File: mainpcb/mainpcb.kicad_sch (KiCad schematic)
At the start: 16 parts, among them J1 Raspberry_Pi_2_3, J13 Screw_Terminal_01x09, J15 Screw_Terminal_01x02, J2 8P8C_Shielded, J3 8P8C_Shielded, J4 Screw_Terminal_01x09, J9 Screw_Terminal_01x02, U1 TCA9517ADGK, U2 TXB0108PW

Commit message: Continued control board layout
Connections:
- net DSCL1+: now also J2.4; no longer J2.5
- net DSCL1-: now also J2.3; no longer J2.6
- net DSCL2+: now also J3.4; no longer J3.5
- net DSCL2-: now also J3.3; no longer J3.6
- net DSDA1+: now also J2.5; no longer J2.3
- net DSDA1-: now also J2.6; no longer J2.4
- net DSDA2+: now also J3.5; no longer J3.3
- net DSDA2-: now also J3.6; no longer J3.4
- net GND: now also J13.2 (Pin_2), J13.9 (Pin_9), J4.2 (Pin_2), J4.9 (Pin_9); no longer J13.1 (Pin_1), J4.1 (Pin_1)
- net at J13.3 (Pin_3): now also U2.14 (B6); no longer U2.12 (B8)
- net at J13.7 (Pin_7): now also U2.12 (B8); no longer U2.14 (B6)
- net at U2.15 (B5): now also J13.1 (Pin_1); no longer J13.9 (Pin_9)
- net at U2.16 (B4): now also J4.7 (Pin_7); no longer J4.3 (Pin_3)
- net at U2.18 (B2): now also J4.3 (Pin_3); no longer J4.7 (Pin_7)
- net at U2.20 (B1): now also J4.1 (Pin_1); no longer J4.9 (Pin_9)
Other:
- moved on the sheet: J13, J4

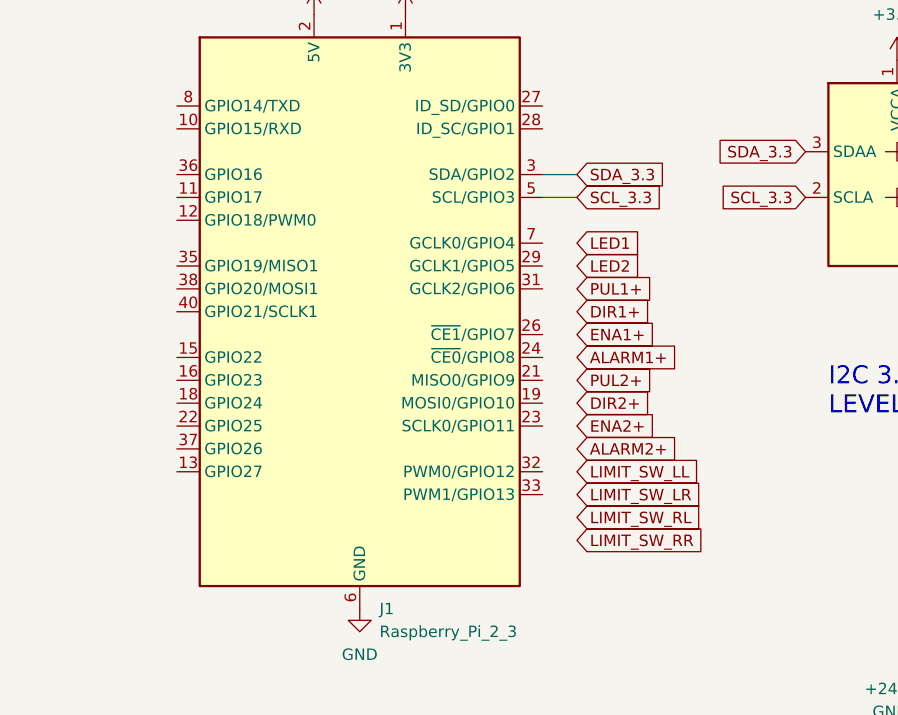
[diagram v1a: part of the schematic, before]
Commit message: Started signal track layout of control PCB
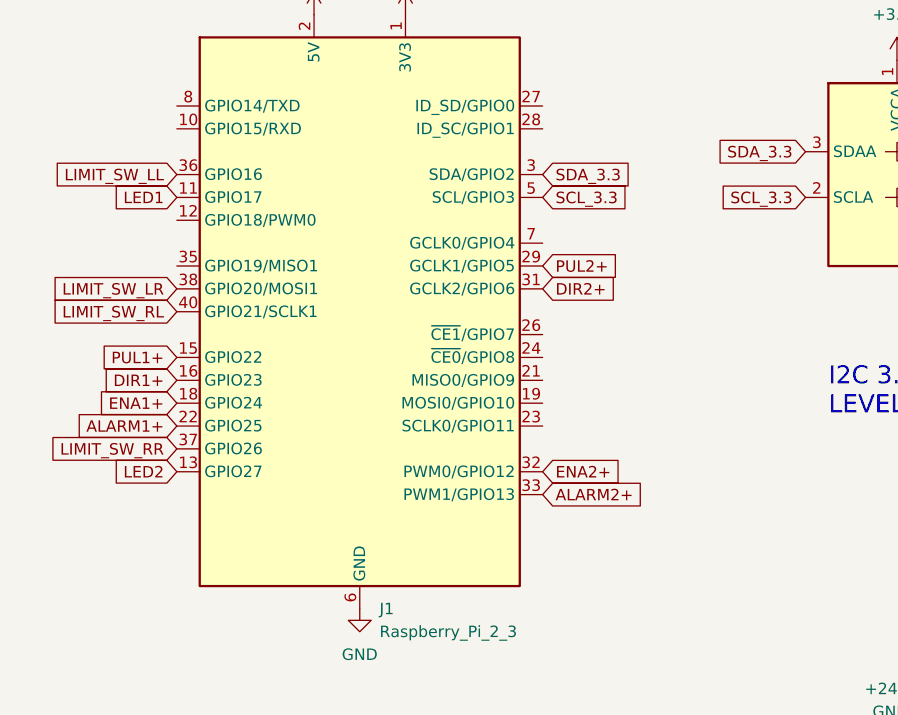
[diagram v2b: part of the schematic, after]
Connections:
- net ALARM1+: now also J1.22 (GPIO25)
- net ALARM2+: now also J1.33 (PWM1/GPIO13)
- net DIR1+: now also J1.16 (GPIO23)
- net DIR2+: now also J1.31 (GCLK2/GPIO6)
- net ENA1+: now also J1.18 (GPIO24)
- net ENA2+: now also J1.32 (PWM0/GPIO12)
- net LED1: now also J1.11 (GPIO17)
- net LED2: now also J1.13 (GPIO27)
- net LIMIT_SW_LL: now also J1.36 (GPIO16)
- net LIMIT_SW_LR: now also J1.38 (GPIO20/MOSI1)
- net LIMIT_SW_RL: now also J1.40 (GPIO21/SCLK1)
- net LIMIT_SW_RR: now also J1.37 (GPIO26)
- net PUL1+: now also J1.15 (GPIO22)
- net PUL2+: now also J1.29 (GCLK1/GPIO5)

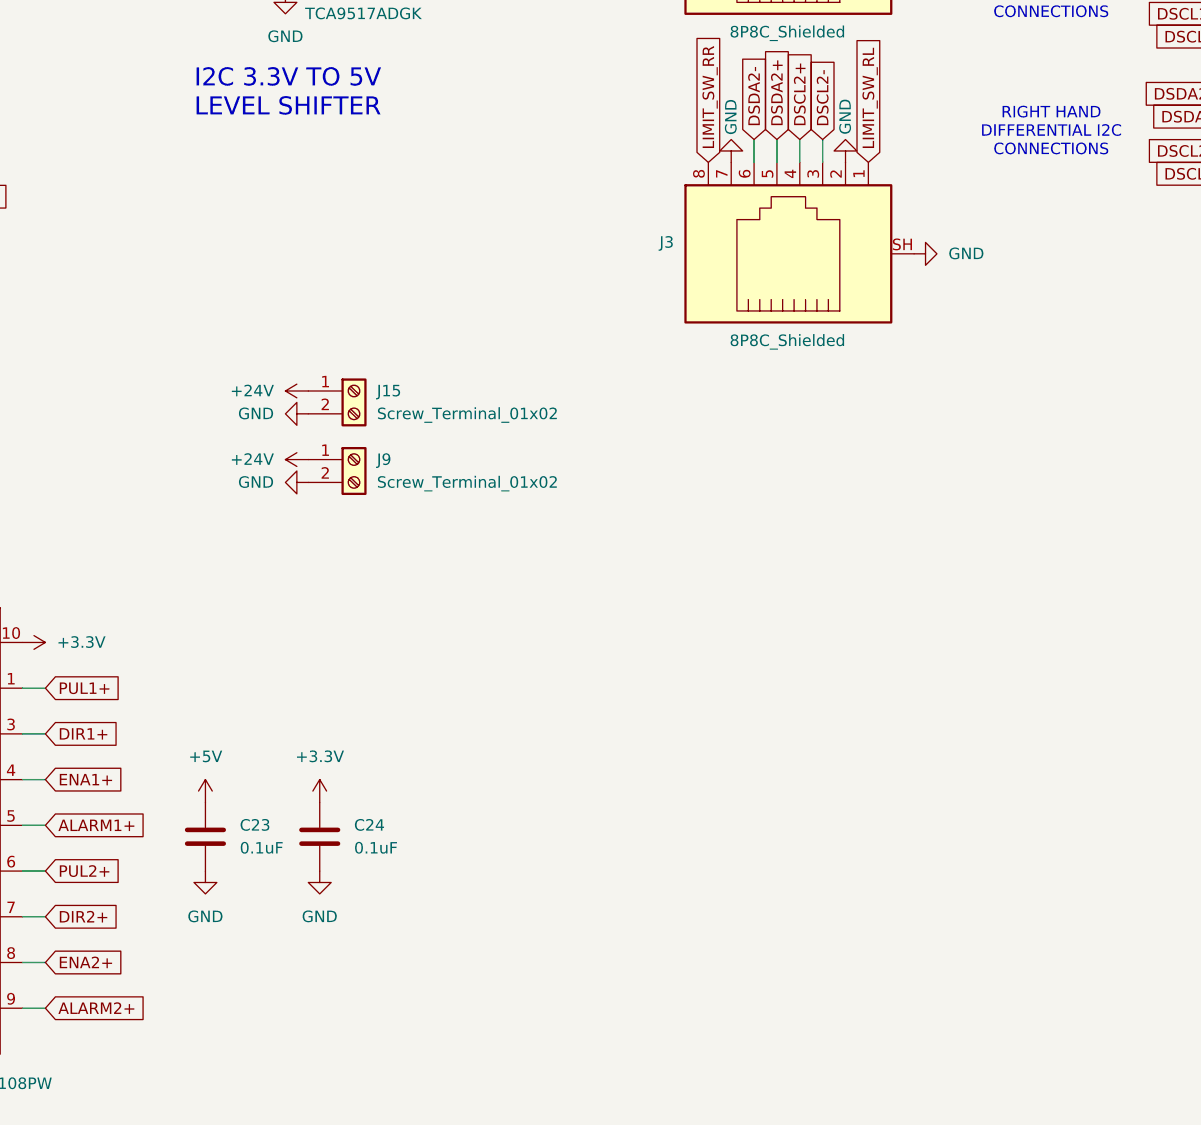
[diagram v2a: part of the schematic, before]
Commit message: Completed control board layout
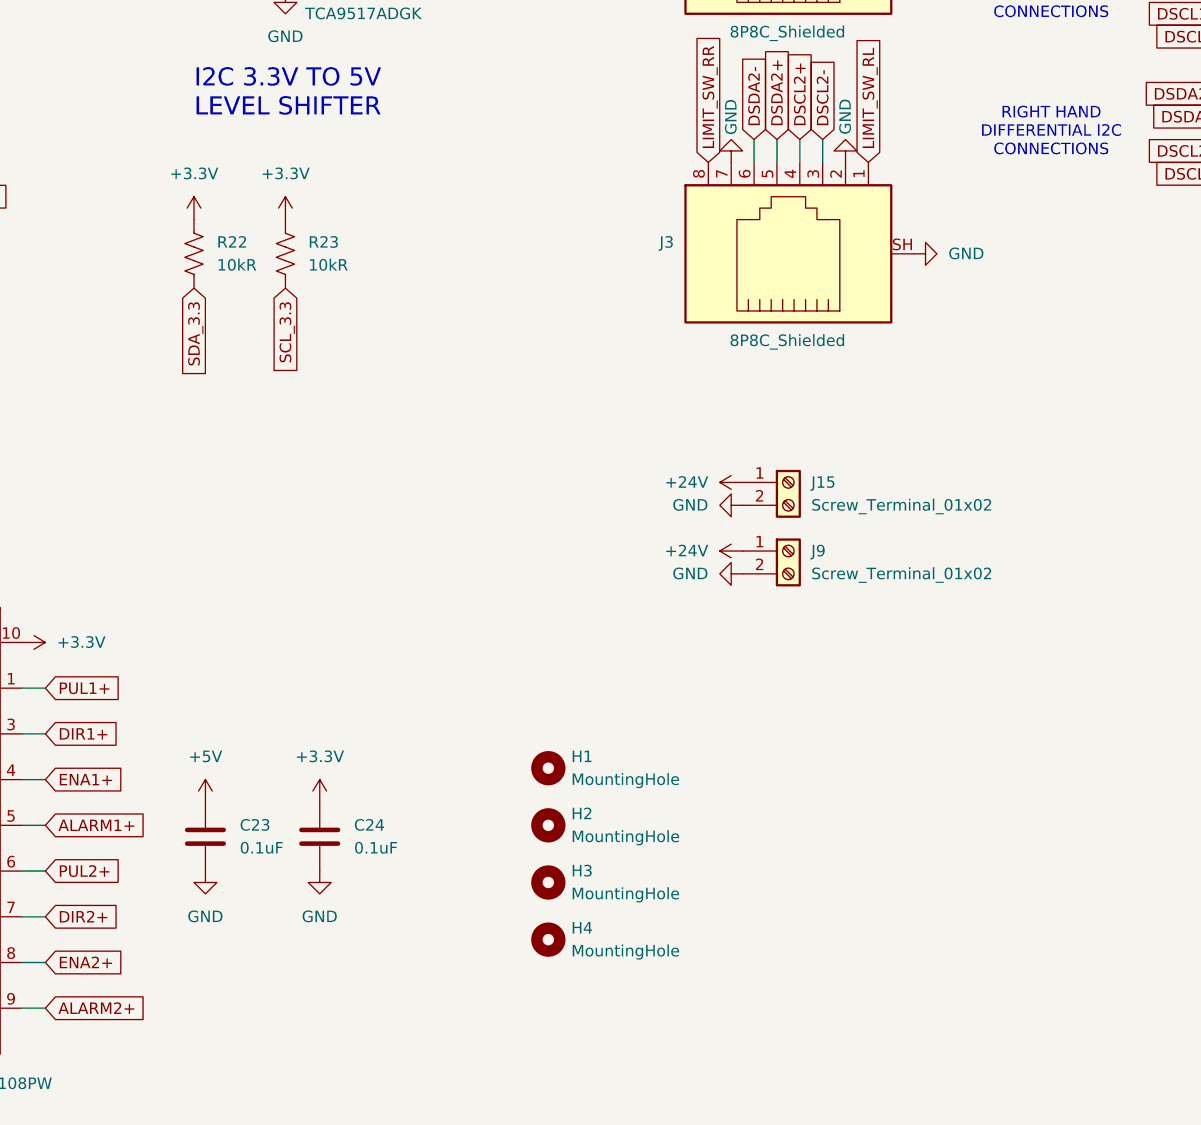
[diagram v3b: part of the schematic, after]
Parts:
- added H1, H2, H3, H4: MountingHole, MountingHole:MountingHole_4.3mm_M4, symbol Mechanical:MountingHole
- added R22, R23: 10kR, Resistor_THT:R_Axial_DIN0207_L6.3mm_D2.5mm_P10.16mm_Horizontal, symbol Device:R_US
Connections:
- net +3.3V: now also R22.1, R23.1
- net SCL_3.3: now also R23.2
- net SDA_3.3: now also R22.2
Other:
- moved on the sheet: J15, J9

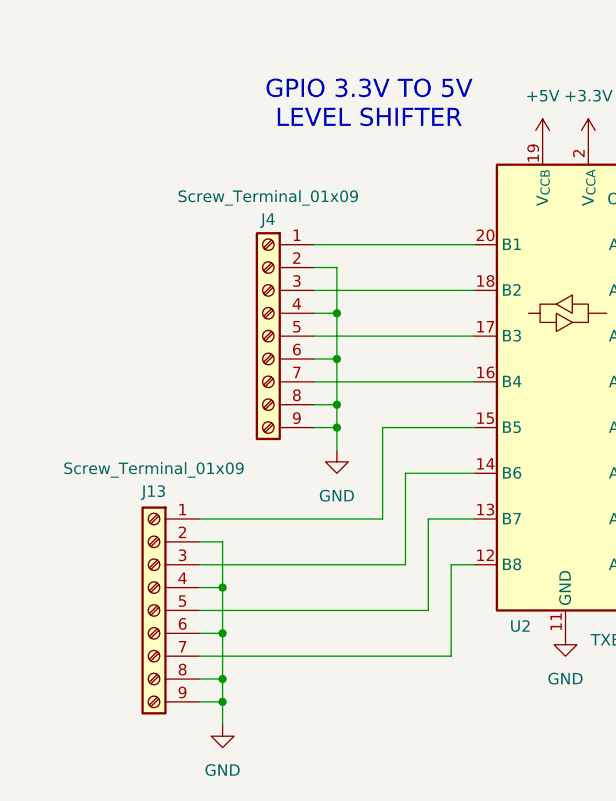
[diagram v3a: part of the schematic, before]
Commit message: As-Produced commit
This commit contains the PCBs as they were sent to the manufacturer
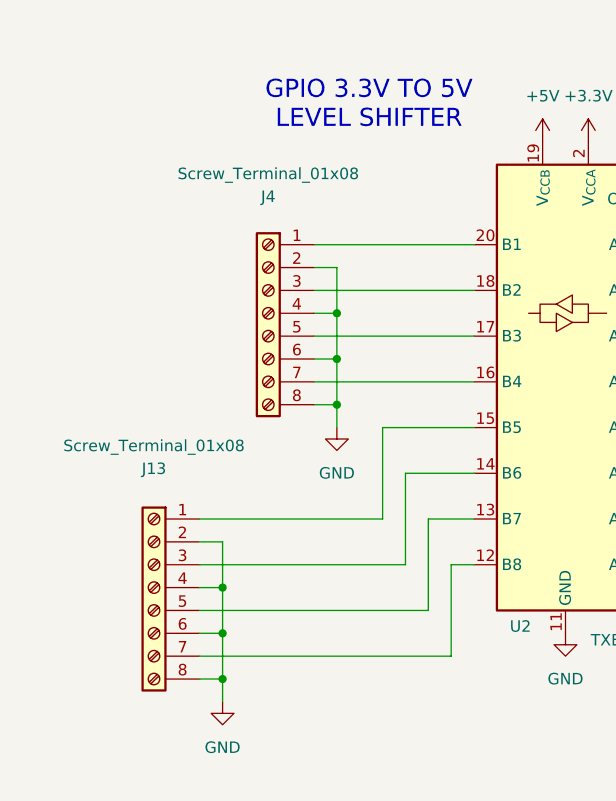
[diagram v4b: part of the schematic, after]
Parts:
- J13, J4: value Screw_Terminal_01x09 -> Screw_Terminal_01x08; footprint TerminalBlock_Phoenix:TerminalBlock_Phoenix_PT-1,5-9-5.0-H_1x09_P5.00mm_Horizontal -> TerminalBlock_Phoenix:TerminalBlock_Phoenix_PT-1,5-8-5.0-H_1x08_P5.00mm_Horizontal; symbol Connector:Screw_Terminal_01x09 -> Connector:Screw_Terminal_01x08; Digikey https://www.digikey.ca/en/products/detail/phoenix-contact/1935239/568621 -> https://www.digikey.ca/en/products/detail/phoenix-contact/1935226/568620
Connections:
- net GND: no longer J13.9 (Pin_9), J4.9 (Pin_9)

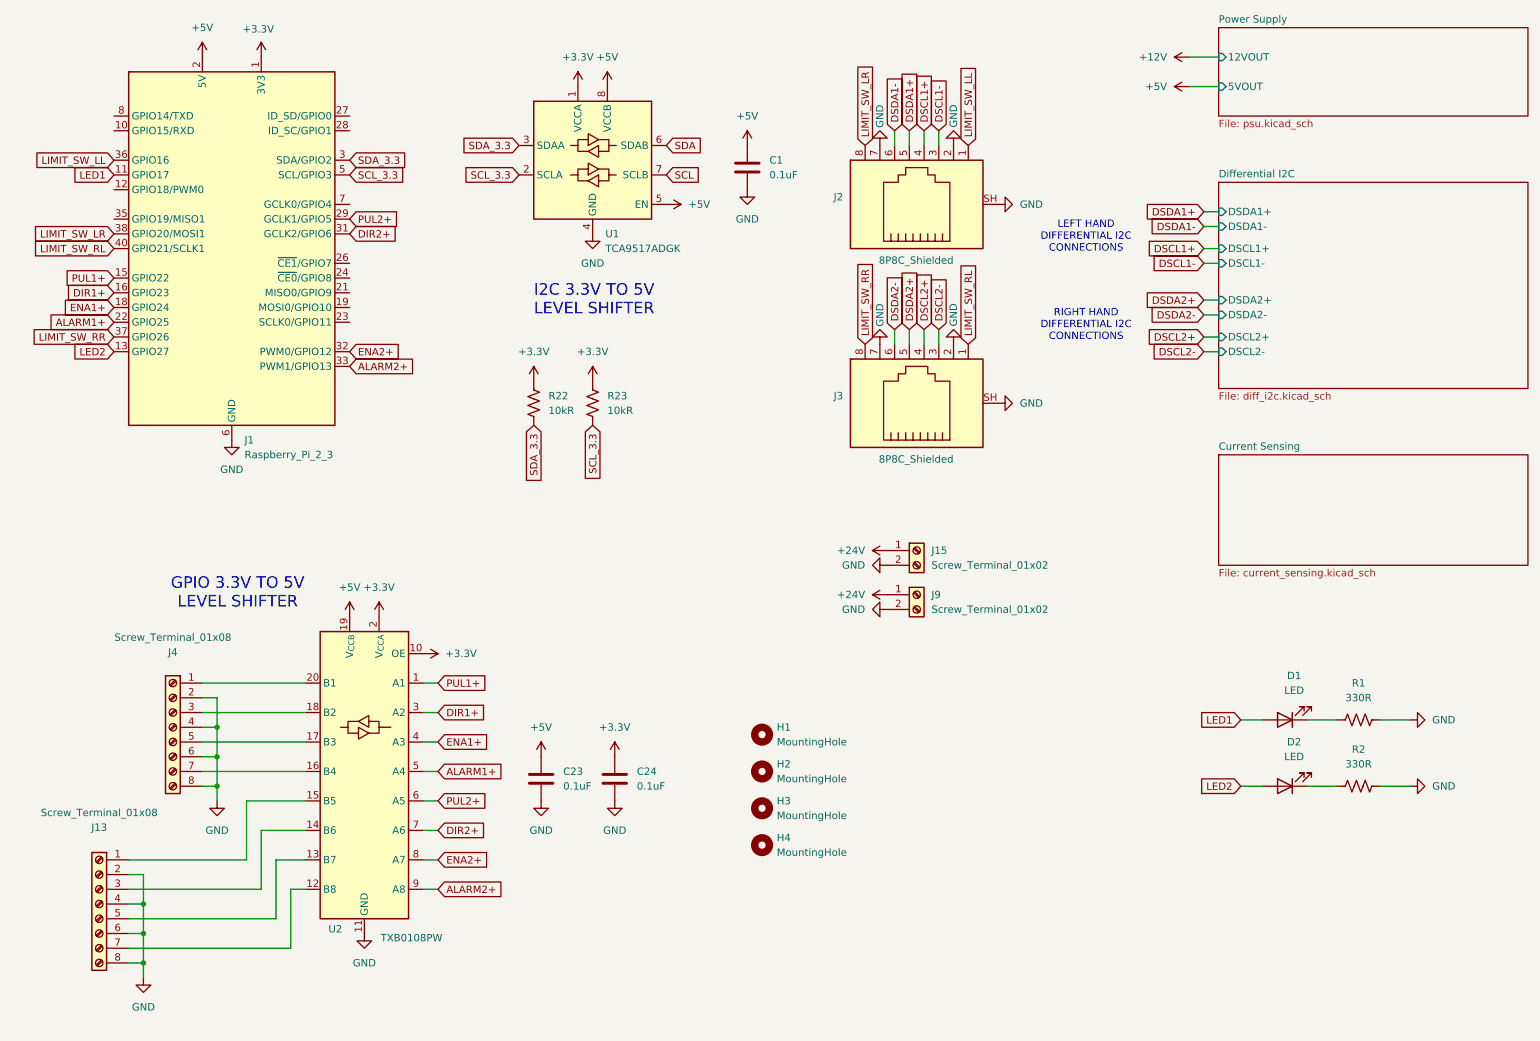
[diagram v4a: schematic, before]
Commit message: Version 1 AS-BUILT commit
This commit has the schematics of version 1 of the system AS IT WAS BUILT
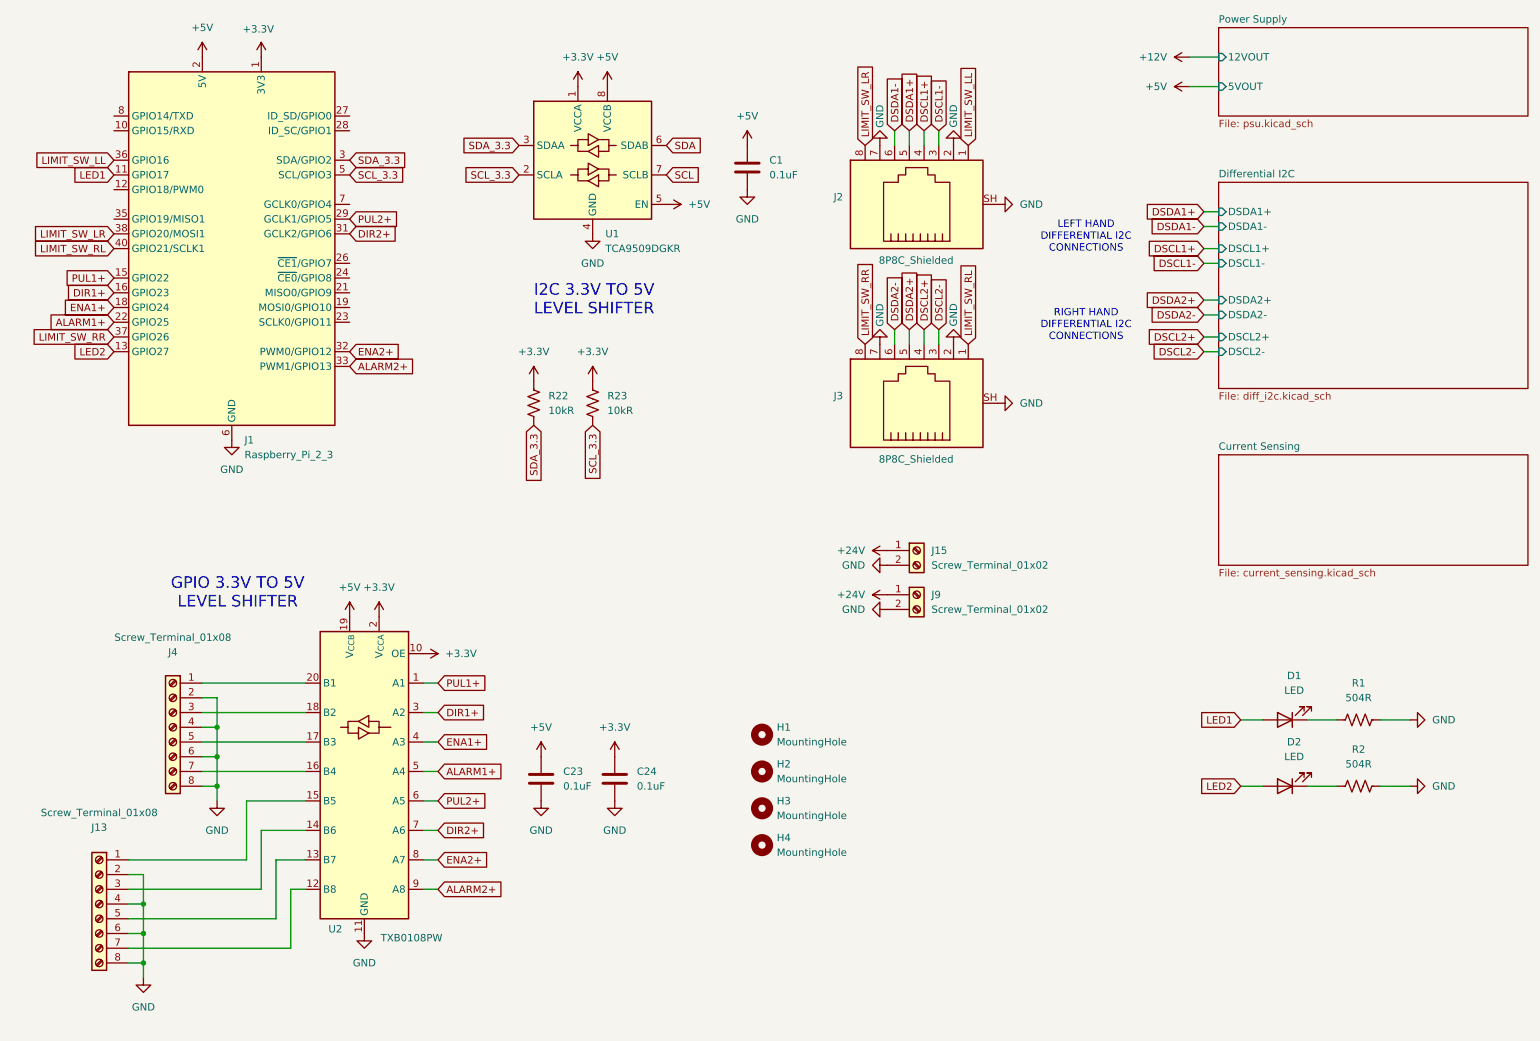
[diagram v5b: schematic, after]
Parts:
- R1, R2: value 330R -> 504R
- U1: value TCA9517ADGK -> TCA9509DGKR
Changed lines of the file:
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@@
 			)
 		)
-		(property "Value" "330R"
+		(property "Value" "504R"
 			(at 247.65 134.62 90)
 			(effects
@@
 			)
 		)
-		(property "Value" "TCA9517ADGK"
+		(property "Value" "TCA9509DGKR"
 			(at 117.7641 57.15 0)
 			(effects
@@
 			)
 		)
-		(property "Datasheet" "https://www.ti.com/lit/ds/symlink/tca9517a.pdf"
+		(property "Datasheet" "https://www.ti.com/lit/ds/symlink/tca9509.pdf"
 			(at 115.57 57.15 0)
 			(effects
@@
 			)
 		)
-		(property "Value" "330R"
+		(property "Value" "504R"
 			(at 247.65 146.05 90)
 			(effects
